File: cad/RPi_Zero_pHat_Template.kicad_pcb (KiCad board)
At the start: 2 copper layers, 65 x 30.5 mm, 6 parts, among them J1 RPi_GPIO, J2 RPi_GPIO

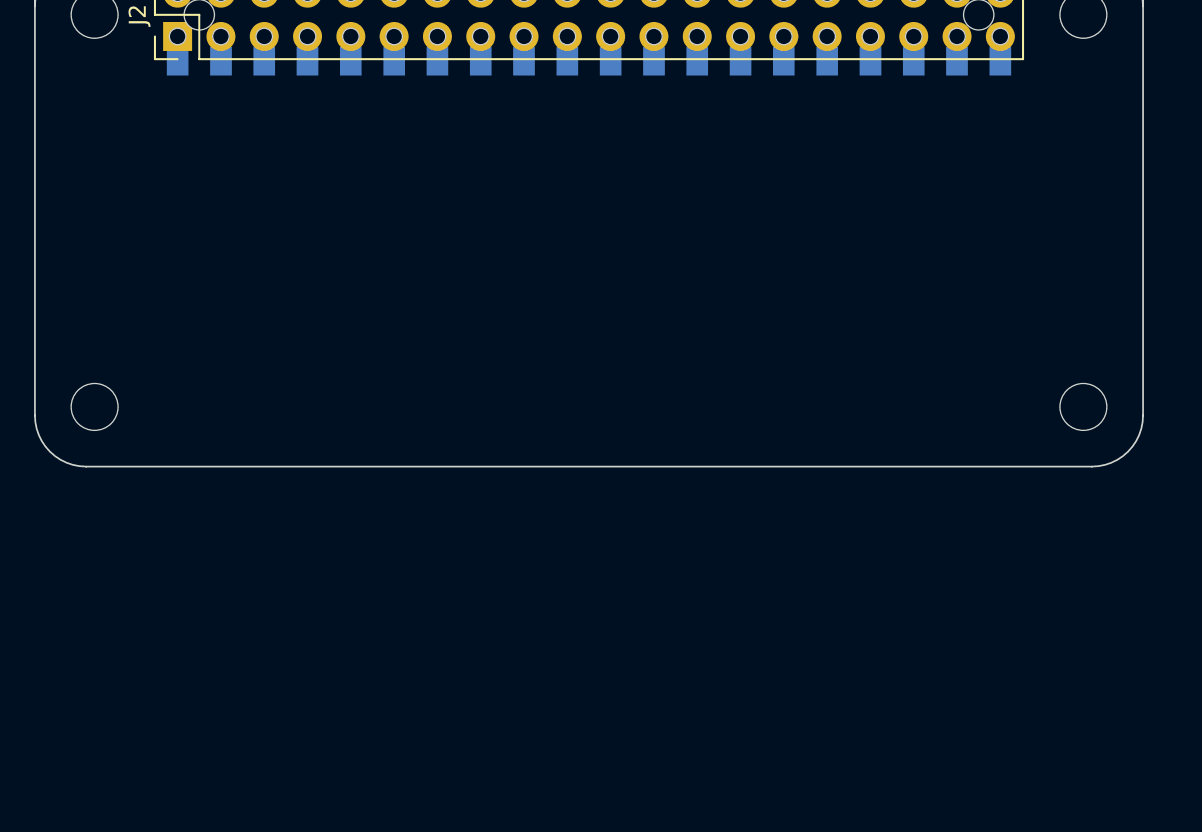
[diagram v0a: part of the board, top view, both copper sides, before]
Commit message: some headers added
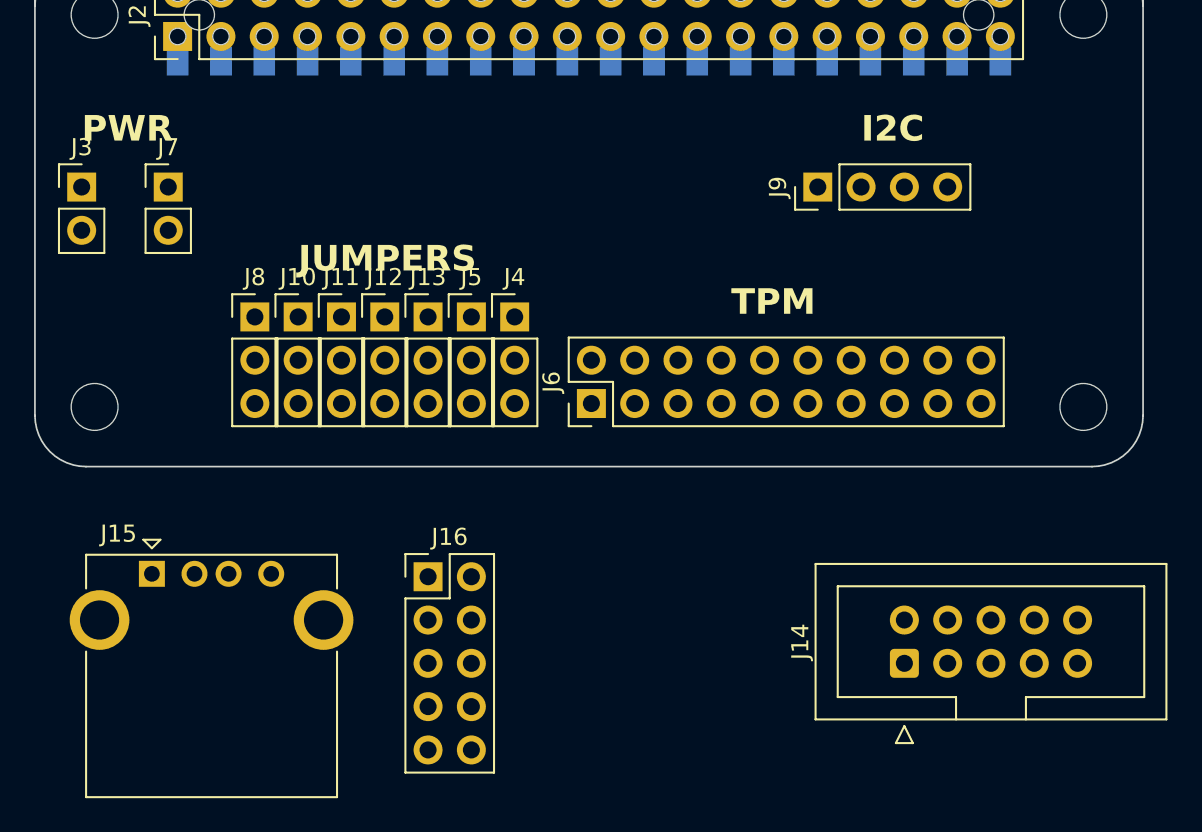
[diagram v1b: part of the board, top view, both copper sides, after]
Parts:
- added J10: Conn_01x03, Connector_PinHeader_2.54mm:PinHeader_1x03_P2.54mm_Vertical, F.Cu at (27.9, 45.7)
- added J11: Conn_01x03, Connector_PinHeader_2.54mm:PinHeader_1x03_P2.54mm_Vertical, F.Cu at (30.5, 45.7)
- added J12: Conn_01x03, Connector_PinHeader_2.54mm:PinHeader_1x03_P2.54mm_Vertical, F.Cu at (33.0, 45.7)
- added J13: Conn_01x03, Connector_PinHeader_2.54mm:PinHeader_1x03_P2.54mm_Vertical, F.Cu at (35.6, 45.7)
- added J14: Conn_02x05_Odd_Even, Connector_IDC:IDC-Header_2x05_P2.54mm_Vertical, F.Cu at (63.5, 66.0)
- added J15: USB_A, Connector_USB:USB_A_CONNFLY_DS1095-WNR0, F.Cu at (19.4, 60.8)
- added J16: Conn_02x05_Odd_Even, Connector_PinHeader_2.54mm:PinHeader_2x05_P2.54mm_Vertical, F.Cu at (35.6, 61.0)
- added J3: Conn_01x02, Connector_PinHeader_2.54mm:PinHeader_1x02_P2.54mm_Vertical, F.Cu at (15.2, 38.1)
- added J4: Conn_01x03, Connector_PinHeader_2.54mm:PinHeader_1x03_P2.54mm_Vertical, F.Cu at (40.6, 45.7)
- added J5: Conn_01x03, Connector_PinHeader_2.54mm:PinHeader_1x03_P2.54mm_Vertical, F.Cu at (38.1, 45.7)
- added J6: Conn_02x10_Odd_Even, Connector_PinHeader_2.54mm:PinHeader_2x10_P2.54mm_Vertical, F.Cu at (45.1, 50.8)
- added J7: Conn_01x02, Connector_PinHeader_2.54mm:PinHeader_1x02_P2.54mm_Vertical, F.Cu at (20.3, 38.1)
- added J8: Conn_01x03, Connector_PinHeader_2.54mm:PinHeader_1x03_P2.54mm_Vertical, F.Cu at (25.4, 45.7)
- added J9: Conn_01x04, Connector_PinHeader_2.54mm:PinHeader_1x04_P2.54mm_Vertical, F.Cu at (58.4, 38.1)
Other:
- board text added: "I2C"
- board text added: "JUMPERS"
- board text added: "PWR"
- board text added: "TPM"

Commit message: init
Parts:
- added D101: led_g, LED_SMD:LED_0603_1608Metric, F.Cu at (51.4, -11.2)
- added D102: led_g, LED_SMD:LED_0603_1608Metric, F.Cu at (54.0, -11.2)
- added D103: led_g, LED_SMD:LED_0603_1608Metric, F.Cu at (56.6, -11.2)
- added D104: led_g, LED_SMD:LED_0603_1608Metric, F.Cu at (59.2, -11.2)
- added D105: led_g, LED_SMD:LED_0603_1608Metric, F.Cu at (61.8, -11.2)
- added D106: led_g, LED_SMD:LED_0603_1608Metric, F.Cu at (51.4, -15.3)
- added D107: led_g, LED_SMD:LED_0603_1608Metric, F.Cu at (54.0, -15.3)
- added D108: led_g, LED_SMD:LED_0603_1608Metric, F.Cu at (56.6, -15.3)
- added D109: led_g, LED_SMD:LED_0603_1608Metric, F.Cu at (56.6, -19.3)
- added D110: led_g, LED_SMD:LED_0603_1608Metric, F.Cu at (59.2, -19.3)
- added D111: led_g, LED_SMD:LED_0603_1608Metric, F.Cu at (59.2, -15.3)
- added D112: led_g, LED_SMD:LED_0603_1608Metric, F.Cu at (61.8, -15.3)
- added D113: led_g, LED_SMD:LED_0603_1608Metric, F.Cu at (51.4, -19.3)
- added D114: led_g, LED_SMD:LED_0603_1608Metric, F.Cu at (54.0, -19.3)
- added J113: power_input, Connector_PinHeader_2.54mm:PinHeader_1x03_P2.54mm_Vertical, F.Cu at (15.5, 11.0)
- added R101: 4.7k, Resistor_SMD:R_0603_1608Metric, F.Cu at (31.3, -11.2)
- added R102: 4.7k, Resistor_SMD:R_0603_1608Metric, F.Cu at (33.8, -11.2)
- added R103: 4.7k, Resistor_SMD:R_0603_1608Metric, F.Cu at (36.3, -11.2)
- added R104: 4.7k, Resistor_SMD:R_0603_1608Metric, F.Cu at (38.8, -11.2)
- added R105: 4.7k, Resistor_SMD:R_0603_1608Metric, F.Cu at (41.3, -11.2)
- added R106: 4.7k, Resistor_SMD:R_0603_1608Metric, F.Cu at (43.8, -11.2)
- added R107: 4.7k, Resistor_SMD:R_0603_1608Metric, F.Cu at (46.4, -11.2)
- added R108: 4.7k, Resistor_SMD:R_0603_1608Metric, F.Cu at (48.9, -11.2)
- added R109: 10k, Resistor_SMD:R_0603_1608Metric, F.Cu at (31.3, -15.2)
- added R110: 10k, Resistor_SMD:R_0603_1608Metric, F.Cu at (33.8, -15.2)
- added R111: 10k, Resistor_SMD:R_0603_1608Metric, F.Cu at (36.3, -15.2)
- added R112: 10k, Resistor_SMD:R_0603_1608Metric, F.Cu at (38.8, -15.2)
- added R113: 10k, Resistor_SMD:R_0603_1608Metric, F.Cu at (41.3, -15.2)
- added R114: 10k, Resistor_SMD:R_0603_1608Metric, F.Cu at (43.8, -15.2)
- added R115: 10k, Resistor_SMD:R_0603_1608Metric, F.Cu at (46.4, -15.2)
- added R116: 10k, Resistor_SMD:R_0603_1608Metric, F.Cu at (48.9, -15.2)
- added R117: 4.7k, Resistor_SMD:R_0603_1608Metric, F.Cu at (41.3, -19.2)
- added R118: 4.7k, Resistor_SMD:R_0603_1608Metric, F.Cu at (43.8, -19.2)
- added R119: 4.7k, Resistor_SMD:R_0603_1608Metric, F.Cu at (31.3, -19.2)
- added R120: 4.7k, Resistor_SMD:R_0603_1608Metric, F.Cu at (33.8, -19.2)
- added R121: 4.7k, Resistor_SMD:R_0603_1608Metric, F.Cu at (36.3, -19.2)
- added R122: 4.7k, Resistor_SMD:R_0603_1608Metric, F.Cu at (38.8, -19.2)
- added R123: 10k, Resistor_SMD:R_0603_1608Metric, F.Cu at (36.3, -23.2)
- added R124: 10k, Resistor_SMD:R_0603_1608Metric, F.Cu at (38.8, -23.2)
- added R125: 10k, Resistor_SMD:R_0603_1608Metric, F.Cu at (46.4, -19.2)
- added R126: 10k, Resistor_SMD:R_0603_1608Metric, F.Cu at (48.9, -19.2)
- added R127: 10k, Resistor_SMD:R_0603_1608Metric, F.Cu at (31.3, -23.2)
- added R128: 10k, Resistor_SMD:R_0603_1608Metric, F.Cu at (33.8, -23.2)
- added U101: ASSR-1218, Package_SO:SO-4_4.4x4.3mm_P2.54mm, F.Cu at (81.5, 17.5)
- added U102: ASSR-1218, Package_SO:SO-4_4.4x4.3mm_P2.54mm, F.Cu at (76.5, 17.5)
- added U103: ASSR-1218, Package_SO:SO-4_4.4x4.3mm_P2.54mm, F.Cu at (71.5, 17.5)
- added U104: ASSR-1218, Package_SO:SO-4_4.4x4.3mm_P2.54mm, F.Cu at (66.5, 17.5)
- added U105: ASSR-1218, Package_SO:SO-4_4.4x4.3mm_P2.54mm, F.Cu at (61.5, 17.5)
- added U106: ASSR-1218, Package_SO:SO-4_4.4x4.3mm_P2.54mm, F.Cu at (56.6, 17.5)
- added U107: ASSR-1218, Package_SO:SO-4_4.4x4.3mm_P2.54mm, F.Cu at (51.5, 17.5)
- added U108: ASSR-1218, Package_SO:SO-4_4.4x4.3mm_P2.54mm, F.Cu at (46.5, 17.5)
- added U109: ASSR-1218, Package_SO:SO-4_4.4x4.3mm_P2.54mm, F.Cu at (21.5, 17.5)
- added U110: ASSR-1218, Package_SO:SO-4_4.4x4.3mm_P2.54mm, F.Cu at (16.5, 17.5)
- added U111: ASSR-1218, Package_SO:SO-4_4.4x4.3mm_P2.54mm, F.Cu at (41.5, 17.5)
- added U112: ASSR-1218, Package_SO:SO-4_4.4x4.3mm_P2.54mm, F.Cu at (36.5, 17.5)
- added U113: ASSR-1218, Package_SO:SO-4_4.4x4.3mm_P2.54mm, F.Cu at (31.5, 17.5)
- added U114: ASSR-1218, Package_SO:SO-4_4.4x4.3mm_P2.54mm, F.Cu at (26.5, 17.5)
- added U115: MCP23017, Package_SO:SOIC-28W_7.5x17.9mm_P1.27mm, F.Cu at (32.4, 3.35)
- moved J115 74.2 mm to (99.2, -0.04), turned to -90 degrees
- moved J108 70.9 mm to (89.3, 48.9), turned to 90 degrees
- moved J105 54.8 mm to (63.1, 6.00), turned to 180 degrees
- moved J101 51.4 mm to (60.6, 6.00), turned to 180 degrees
- moved J111 51.4 mm to (82.5, 40.0)
- moved J116 48.6 mm to (96.0, 30.0), turned to -90 degrees
- moved J104 48.3 mm to (58.0, 6.00), turned to 180 degrees
- moved J102 45.6 mm to (55.5, 6.00), turned to 180 degrees
- moved J107 43.4 mm to (53.0, 6.00), turned to 180 degrees
- moved J103 41.6 mm to (50.4, 6.00), turned to 180 degrees
- moved J106 40.4 mm to (47.9, 6.00), turned to 180 degrees
- moved J110 38.4 mm to (19.5, -0.28)
- moved J109 38.1 mm to (15.5, -0.04)
- moved J112 34.9 mm to (89.9, 23.0)
- renumbered J10 to J101, J12 to J102, J5 to J103, J11 to J104, J8 to J105, J4 to J106, J13 to J107, J15 to J108, J3 to J109, J7 to J110, J16 to J111, J9 to J112, J6 to J115, J14 to J116
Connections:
- J101 pad 1: unconnected-(J10-Pin_1-Pad1) -> Net-(J101-Pin_1)
- J101 pad 2: unconnected-(J10-Pin_2-Pad2) -> Net-(J101-Pin_2)
- J101 pad 3: unconnected-(J10-Pin_3-Pad3) -> Net-(J101-Pin_3)
- J102 pad 1: unconnected-(J12-Pin_1-Pad1) -> Net-(J102-Pin_1)
- J102 pad 2: unconnected-(J12-Pin_2-Pad2) -> Net-(J102-Pin_2)
- J102 pad 3: unconnected-(J12-Pin_3-Pad3) -> Net-(J102-Pin_3)
- J103 pad 1: unconnected-(J5-Pin_1-Pad1) -> Net-(J103-Pin_1)
- J103 pad 2: unconnected-(J5-Pin_2-Pad2) -> Net-(J103-Pin_2)
- J103 pad 3: unconnected-(J5-Pin_3-Pad3) -> Net-(J103-Pin_3)
- J104 pad 1: unconnected-(J11-Pin_1-Pad1) -> Net-(J104-Pin_1)
- J104 pad 2: unconnected-(J11-Pin_2-Pad2) -> Net-(J104-Pin_2)
- J104 pad 3: unconnected-(J11-Pin_3-Pad3) -> Net-(J104-Pin_3)
- J105 pad 1: unconnected-(J8-Pin_1-Pad1) -> Net-(J105-Pin_1)
- J105 pad 2: unconnected-(J8-Pin_2-Pad2) -> Net-(J105-Pin_2)
- J105 pad 3: unconnected-(J8-Pin_3-Pad3) -> Net-(J105-Pin_3)
- J106 pad 1: unconnected-(J4-Pin_1-Pad1) -> Net-(J106-Pin_1)
- J106 pad 2: unconnected-(J4-Pin_2-Pad2) -> Net-(J106-Pin_2)
- J106 pad 3: unconnected-(J4-Pin_3-Pad3) -> Net-(J106-Pin_3)
- J107 pad 1: unconnected-(J13-Pin_1-Pad1) -> Net-(J107-Pin_1)
- J107 pad 2: unconnected-(J13-Pin_2-Pad2) -> Net-(J107-Pin_2)
- J107 pad 3: unconnected-(J13-Pin_3-Pad3) -> Net-(J107-Pin_3)
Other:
- board size 65 x 30.5 mm -> 90 x 58 mm

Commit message: check in before tpm
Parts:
- removed D101, D102, D103, D104, D105, D106, D107, D108, D109, D110, D111, D112, D113, D114: led_g, LED_SMD:LED_0603_1608Metric
- removed J1: RPi_GPIO, Connector_Samtec_HLE_SMD-ML:Samtec_HLE-120-02-xxx-DV-BE-A_2x20_RPi_Bottom
- removed J2: RPi_GPIO, Connector_PinHeader_2.54mm:PinHeader_2x20_P2.54mm_Vertical
- removed R109, R110, R111, R112, R113, R114, R115, R116, R123, R124, R125, R126, R127, R128: 10k, Resistor_SMD:R_0603_1608Metric
- added C101: .1uF, Capacitor_SMD:C_0603_1608Metric, F.Cu at (35.0, 11.0)
- added C102: 22uF, Capacitor_SMD:C_0805_2012Metric, F.Cu at (18.6, 6.43)
- added J115: RPi_GPIO, Connector_PinHeader_2.54mm:PinHeader_2x20_P2.54mm_Vertical, F.Cu at (20.9, 29.3)
- added JP101: Jumper_NC_Small, Jumper:SolderJumper-2_P1.3mm_Bridged_RoundedPad1.0x1.5mm, B.Cu at (80.1, 39.7)
- added JP102: Jumper_NC_Small, Jumper:SolderJumper-2_P1.3mm_Bridged_RoundedPad1.0x1.5mm, B.Cu at (80.2, 37.1)
- added R129: 4.7k, Resistor_SMD:R_0603_1608Metric, F.Cu at (22.0, 14.3)
- added R130: 4.7k, Resistor_SMD:R_0603_1608Metric, F.Cu at (16.7, 14.2)
- added R131: 4.7k, Resistor_SMD:R_0603_1608Metric, F.Cu at (80.1, 39.1)
- added R132: 4.7k, Resistor_SMD:R_0603_1608Metric, F.Cu at (80.1, 37.5)
- added R133: 4.7k, Resistor_SMD:R_0603_1608Metric, F.Cu at (9.95, 34.2)
- added R134: 4.7k, Resistor_SMD:R_0603_1608Metric, F.Cu at (11.4, 34.1)
- added U115: ASSR-1218, Package_SO:SO-4_4.4x4.3mm_P2.54mm, F.Cu at (20.7, 19.0)
- added U116: ASSR-1218, Package_SO:SO-4_4.4x4.3mm_P2.54mm, F.Cu at (15.5, 19.0)
- moved U110 74.5 mm to (91.0, 19.0), turned to -90 degrees
- moved U109 64.5 mm to (86.0, 19.0), turned to -90 degrees
- moved R118 58.7 mm to (92.1, 14.2), turned to 180 degrees
- moved R117 57.0 mm to (87.8, 13.9), turned to 180 degrees
- moved U101 55.5 mm to (26.0, 19.0), turned to -90 degrees
- moved U114 54.5 mm to (81.0, 19.0), turned to -90 degrees
- moved R122 53.8 mm to (81.6, 13.4), turned to 180 degrees
- moved R121 52.8 mm to (77.9, 13.3), turned to 0 degrees
- moved R120 51.0 mm to (72.2, 14.3), turned to 180 degrees
- moved R119 49.6 mm to (68.6, 13.4), turned to 0 degrees
- moved U102 45.5 mm to (31.0, 19.0), turned to -90 degrees
- moved U113 44.5 mm to (76.0, 19.0), turned to -90 degrees
- moved U103 35.5 mm to (36.0, 19.0), turned to -90 degrees
- moved U112 34.5 mm to (71.0, 19.0), turned to -90 degrees
- moved R108 28.5 mm to (61.9, 14.2), turned to 180 degrees
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- renumbered J116 to J108, J110 to J109, J109 to J110, J112 to J111, J108 to J112, J111 to J113, J113 to J114, J115 to J116, U115 to U117
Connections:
- J108 pad 3: unconnected-(J116-Pin_3-Pad3) (its old number) -> /RX
- J108 pad 5: unconnected-(J116-Pin_5-Pad5) (its old number) -> /TX
- J109 pad 1: unconnected-(J110-Pin_1-Pad1) -> Net-(J109-Pin_1)
- J109 pad 2: unconnected-(J110-Pin_2-Pad2) -> Net-(J109-Pin_2)
- J110 pad 1: unconnected-(J109-Pin_1-Pad1) -> Net-(J110-Pin_1)
- J110 pad 2: unconnected-(J109-Pin_2-Pad2) -> Net-(J110-Pin_2)
- J111 pad 1: unconnected-(J112-Pin_1-Pad1) -> /SDA
- J111 pad 2: unconnected-(J112-Pin_2-Pad2) -> GND
- J111 pad 3: unconnected-(J112-Pin_3-Pad3) -> /SCL
- J112 pad 2: unconnected-(J108-D--Pad2) -> Net-(J112-D-)
- J112 pad 3: unconnected-(J108-D+-Pad3) -> Net-(J112-D+)
- J112 pad 4: unconnected-(J108-GND-Pad4) -> GND
- J112 pad 5: unconnected-(J108-Shield-Pad5) -> GND
- J113 pad 3: unconnected-(J111-Pin_3-Pad3) -> Net-(J112-D-)
- J113 pad 5: unconnected-(J111-Pin_5-Pad5) -> Net-(J112-D+)
- R101 pad 2: unconnected-(R101-Pad2) -> /E_GPB0
- R102 pad 2: Net-(D102-A) -> /E_GPB1
- R103 pad 2: unconnected-(R103-Pad2) -> /E_GPB2
- R104 pad 2: Net-(D104-A) -> /E_GPB3
- R105 pad 2: unconnected-(R105-Pad2) -> /E_GPB4
- R106 pad 2: Net-(D106-A) -> /E_GPB5
- R107 pad 2: unconnected-(R107-Pad2) -> /E_GPB7
- R108 pad 2: Net-(D108-A) -> /E_GPB6
- R117 pad 2: unconnected-(R117-Pad2) -> /E_GPA1
- R118 pad 2: Net-(D110-A) -> /E_GPA0
- R119 pad 2: unconnected-(R119-Pad2) -> /E_GPA5
- R120 pad 2: Net-(D112-A) -> /E_GPA4
- R121 pad 2: unconnected-(R121-Pad2) -> /E_GPA3
- R122 pad 2: Net-(D114-A) -> /E_GPA2
- U117 pad 12: /TWI1_SCK -> /IO_SCL
- U117 pad 13: /TWI1_SDA -> /IO_SDA
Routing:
- net +3V3: track 0.00 -> 128.6 mm, vias 0 -> 5
- net /SDA: track 0.00 -> 118.4 mm, vias 0 -> 1
- net /SCL: track 0.00 -> 110.6 mm, vias 0 -> 2
- net /IO_SDA: track 0.00 -> 90.9 mm, vias 0 -> 4
- net /IO_SCL: track 0.00 -> 85.0 mm, vias 0 -> 4
- net /E_GPA0: track 0.00 -> 68.8 mm
- net /E_GPA2: track 0.00 -> 68.3 mm, vias 0 -> 2
- net /E_GPA3: track 0.00 -> 68.2 mm, vias 0 -> 2
- net /E_GPA1: track 0.00 -> 67.2 mm
- net /RX: track 0.00 -> 66.5 mm, vias 0 -> 1
- net /TX: track 0.00 -> 66.1 mm
- net /E_GPA5: track 0.00 -> 64.7 mm, vias 0 -> 2
- net /E_GPA4: track 0.00 -> 63.4 mm, vias 0 -> 2
- net Net-(J105-Pin_2): track 0.00 -> 40.2 mm, vias 0 -> 1
- net /E_GPB6: track 0.00 -> 37.3 mm, vias 0 -> 2
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- added copper zone on B.Cu, net GND
- added copper zone on F.Cu, net GND
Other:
- board size 90 x 58 mm -> 95 x 58 mm
- board text added: "*"
- board text added: "+5V"
- board text added: "1"
- board text added: "2"
- board text added: "3"
- board text added: "CUT JUMPERS TO REMOVE PULLUPS"
- board text added: "GND"
- board text added: "JBR1"
- board text added: "JI2C1"
- board text added: "JI2C2"
- board text added: "JPB1"
- board text added: "JPG1"
- board text added: "JPME1"
- board text added: "JPME2"
- board text added: "NC"
- board text added: "PWR INPUT"
- board text added: "RESET"
- board text added: "SCL"
- board text added: "SDA"
- board text added: "locked"
- board text added: "wakeup"
- board text removed: "PWR"
- board text removed: "Select one of these board edges depending upon the type of socket that is used."

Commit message: rev 0.1
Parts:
- added JP103: Jumper_NC_Small, Jumper:SolderJumper-2_P1.3mm_Bridged_RoundedPad1.0x1.5mm, B.Cu at (79.1, 24.7)
- moved J116 27.8 mm to (102.9, 27.5)
- moved J108 26.9 mm to (97.7, 0.56)
- moved JP102 13.8 mm to (83.8, 50.4)
- moved R132 13.2 mm to (83.8, 50.2), turned to 180 degrees
- moved J111 11.3 mm to (101.5, 9.74), turned to -90 degrees
- moved R131 9.66 mm to (83.8, 48.0), turned to 180 degrees
- moved JP101 8.86 mm to (83.8, 47.7)
- moved J112 5.14 mm to (92.1, 41.9)
- moved J113 5.14 mm to (90.9, 38.3)
- moved R104 0.83 mm to (41.3, 14.3)
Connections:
- J114 pad 2: GND -> unconnected-(J114-Pin_2-Pad2)
- J115 pad 24: unconnected-(J115-GPIO08_SPI_CE0_N-Pad24) -> /LFRAME
- J115 pad 26: unconnected-(J115-GPIO07_SPI_CE1_N-Pad26) -> /LRESET
- J115 pad 29: unconnected-(J115-GPIO05-Pad29) -> /LAD2
- J115 pad 31: unconnected-(J115-GPIO06-Pad31) -> /LAD1
- J115 pad 32: unconnected-(J115-GPIO12-Pad32) -> /LAD3
- J115 pad 33: unconnected-(J115-GPIO13-Pad33) -> /SMB_DAT
- J115 pad 35: unconnected-(J115-GPIO19-Pad35) -> /SER_IRQ
- J115 pad 36: unconnected-(J115-GPIO16-Pad36) -> /LAD0
- J115 pad 37: unconnected-(J115-GPIO26-Pad37) -> /LDRQ
- J115 pad 38: unconnected-(J115-GPIO20-Pad38) -> /SMB_CLK
- J115 pad 40: unconnected-(J115-GPIO21-Pad40) -> /LPCPD
- J116 pad 10: unconnected-(J116-Pin_10-Pad10) -> /LAD1
- J116 pad 11: unconnected-(J116-Pin_11-Pad11) -> /LAD0
- J116 pad 12: unconnected-(J116-Pin_12-Pad12) -> GND
- J116 pad 13: unconnected-(J116-Pin_13-Pad13) -> /SMB_CLK
- J116 pad 14: unconnected-(J116-Pin_14-Pad14) -> /SMB_DAT
- J116 pad 16: unconnected-(J116-Pin_16-Pad16) -> /SER_IRQ
- J116 pad 17: unconnected-(J116-Pin_17-Pad17) -> GND
- J116 pad 18: unconnected-(J116-Pin_18-Pad18) -> GND
- J116 pad 19: unconnected-(J116-Pin_19-Pad19) -> Net-(J116-Pin_19)
- J116 pad 2: unconnected-(J116-Pin_2-Pad2) -> GND
- J116 pad 20: unconnected-(J116-Pin_20-Pad20) -> /LDRQ
- J116 pad 3: unconnected-(J116-Pin_3-Pad3) -> /LFRAME
- J116 pad 5: unconnected-(J116-Pin_5-Pad5) -> /LRESET
- J116 pad 7: unconnected-(J116-Pin_7-Pad7) -> /LAD3
- J116 pad 8: unconnected-(J116-Pin_8-Pad8) -> /LAD2
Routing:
- net /LRESET: track 0.00 -> 60.0 mm
- net /LFRAME: track 0.00 -> 55.2 mm
- net /LAD3: track 0.00 -> 48.6 mm
- net /TX: track 66.1 -> 111.2 mm, vias 0 -> 2
- net /LAD2: track 0.00 -> 44.5 mm
- net /LAD0: track 0.00 -> 43.1 mm
- net /LAD1: track 0.00 -> 38.7 mm
- net /RX: track 66.5 -> 104.6 mm, vias 1 -> 2
- net /SMB_CLK: track 0.00 -> 31.6 mm
- net /SMB_DAT: track 0.00 -> 30.3 mm
- net /SER_IRQ: track 0.00 -> 24.9 mm
- net /SCL: track 110.6 -> 133.6 mm
- net /SDA: track 118.4 -> 138.2 mm
- net /LDRQ: track 0.00 -> 18.0 mm
- net +3V3: track 128.6 -> 143.1 mm
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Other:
- board size 95 x 58 mm -> 100 x 58 mm
- board text added: "COM PORT"
- board text added: "CUT JUMPERS TO REMOVE 3V3 STBY"
- board text added: "USB"

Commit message: move spi pins
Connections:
- J115 pad 19: unconnected-(J115-GPIO10_SPI_MOSI-Pad19) -> /LAD1
- J115 pad 21: unconnected-(J115-GPIO09_SPI_MISO-Pad21) -> /LAD0
- J115 pad 23: unconnected-(J115-GPIO11_SPI_CLK-Pad23) -> /LCLK
- J115 pad 31: /LAD1 -> unconnected-(J115-GPIO06-Pad31)
- J115 pad 36: /LAD0 -> unconnected-(J115-GPIO16-Pad36)
- J116 pad 1: unconnected-(J116-Pin_1-Pad1) -> /LCLK
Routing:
- net /LCLK: track 0.00 -> 62.7 mm
- net /LAD1: track 38.7 -> 53.9 mm, vias 0 -> 2
- net /LAD0: track 43.1 -> 50.8 mm, vias 0 -> 2
- net unconnected-(J115-GPIO16-Pad36): track 0.00 -> 0.72 mm
- net GND: vias 178 -> 188

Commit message: add led
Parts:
- added D115: led_g, LED_SMD:LED_0603_1608Metric, F.Cu at (85.0, 37.0)
- added R132: 4.7k, Resistor_SMD:R_0603_1608Metric, F.Cu at (85.0, 38.7)
- renumbered R132 to R133, R133 to R134, R134 to R135
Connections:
- J115 pad 18: unconnected-(J115-GPIO24-Pad18) -> /LED
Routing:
- net /LED: track 0.00 -> 50.2 mm
- net Net-(D115-A): track 0.00 -> 1.71 mm
- net GND: vias 188 -> 191
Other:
- board text added: "LED"
